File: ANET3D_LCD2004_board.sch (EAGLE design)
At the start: 15 parts

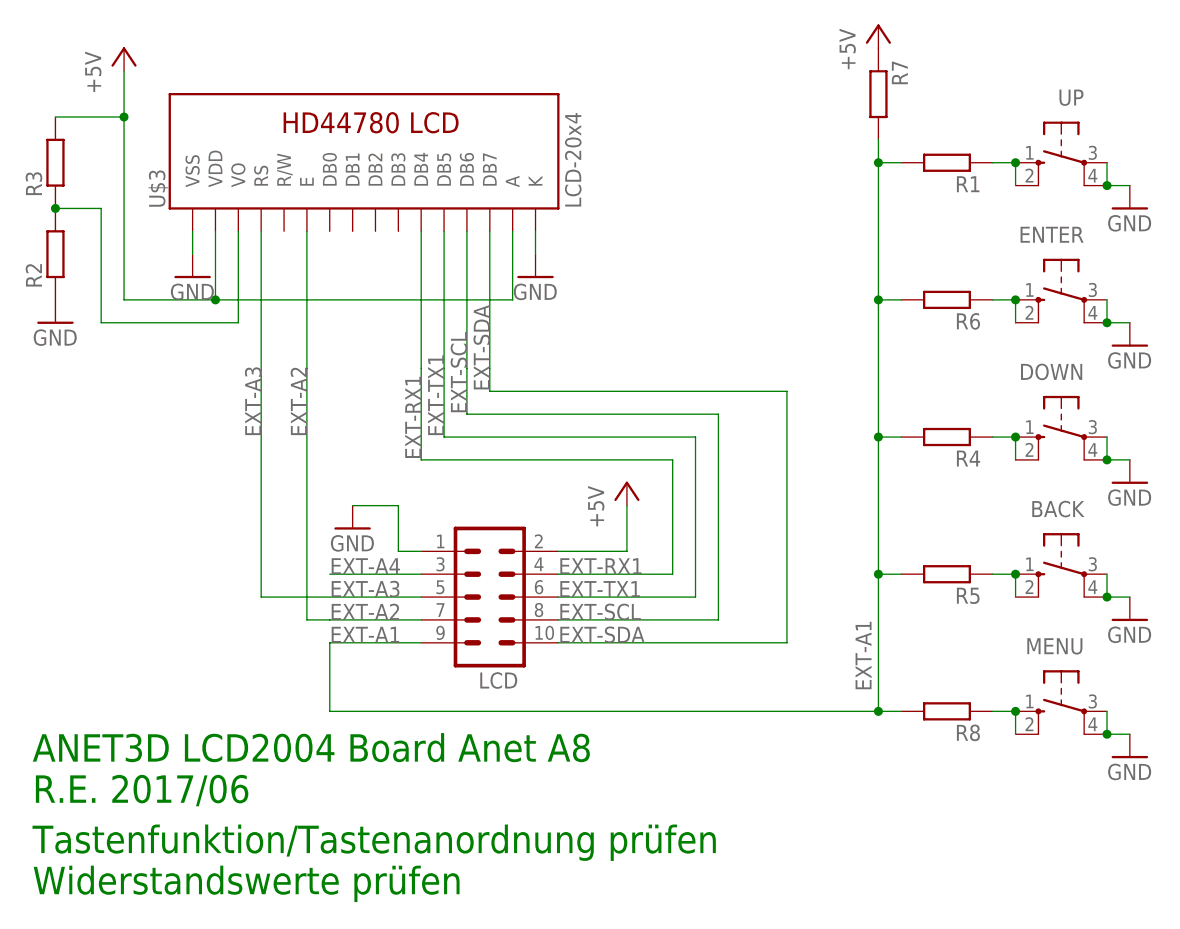
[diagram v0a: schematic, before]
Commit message: LCD2004 keypad resistor values
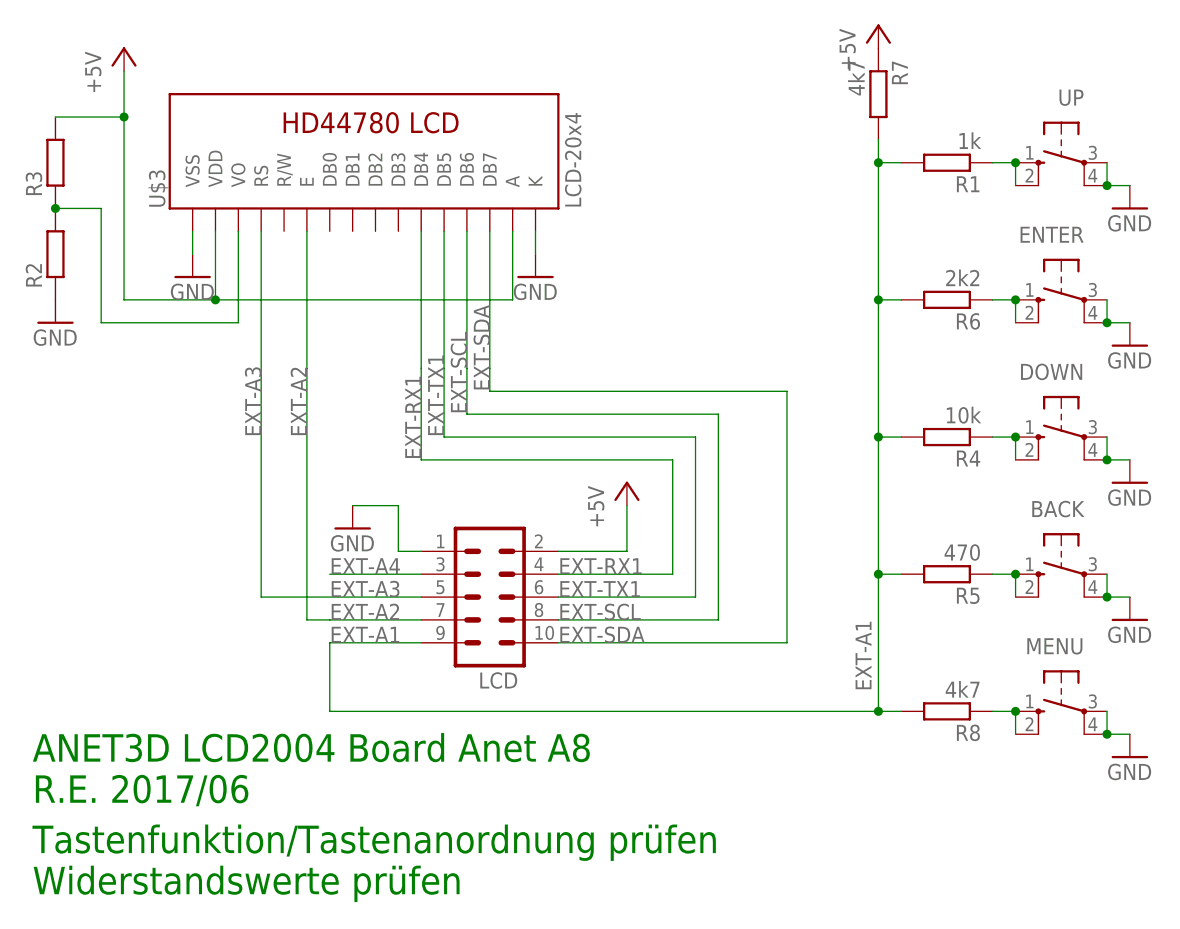
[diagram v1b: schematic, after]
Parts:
- R1: value (none) -> 1k
- R4: value (none) -> 10k
- R5: value (none) -> 470
- R6: value (none) -> 2k2
- R7, R8: value (none) -> 4k7
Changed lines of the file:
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@@
 <part name="R2" library="rcl" deviceset="R-EU_" device="R0805"/>
 <part name="R3" library="rcl" deviceset="R-EU_" device="R0805"/>
-<part name="R4" library="rcl" deviceset="R-EU_" device="R0805"/>
-<part name="R5" library="rcl" deviceset="R-EU_" device="R0805"/>
-<part name="R6" library="rcl" deviceset="R-EU_" device="R0805"/>
+<part name="R4" library="rcl" deviceset="R-EU_" device="R0805" value="10k"/>
+<part name="R5" library="rcl" deviceset="R-EU_" device="R0805" value="470"/>
+<part name="R6" library="rcl" deviceset="R-EU_" device="R0805" value="2k2"/>
 <part name="BACK" library="switch-omron" deviceset="40-XX" device=""/>
 <part name="MENU" library="switch-omron" deviceset="40-XX" device=""/>
@@
 <part name="UP" library="switch-omron" deviceset="40-XX" device=""/>
 <part name="DOWN" library="switch-omron" deviceset="40-XX" device=""/>
-<part name="R1" library="rcl" deviceset="R-EU_" device="R0805"/>
+<part name="R1" library="rcl" deviceset="R-EU_" device="R0805" value="1k"/>
 <part name="GND1" library="SparkFun" deviceset="GND" device=""/>
 <part name="GND2" library="SparkFun" deviceset="GND" device=""/>
@@
 <part name="GND8" library="SparkFun" deviceset="GND" device=""/>
 <part name="P+4" library="supply1" deviceset="+5V" device=""/>
-<part name="R8" library="rcl" deviceset="R-EU_" device="R0805"/>
-<part name="R7" library="rcl" deviceset="R-EU_" device="R0805"/>
+<part name="R8" library="rcl" deviceset="R-EU_" device="R0805" value="4k7"/>
+<part name="R7" library="rcl" deviceset="R-EU_" device="R0805" value="4k7"/>
 <part name="GND9" library="SparkFun" deviceset="GND" device=""/>
 <part name="GND10" library="SparkFun" deviceset="GND" device=""/>

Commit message: Anet3d LCD2004 Resistor values corrected
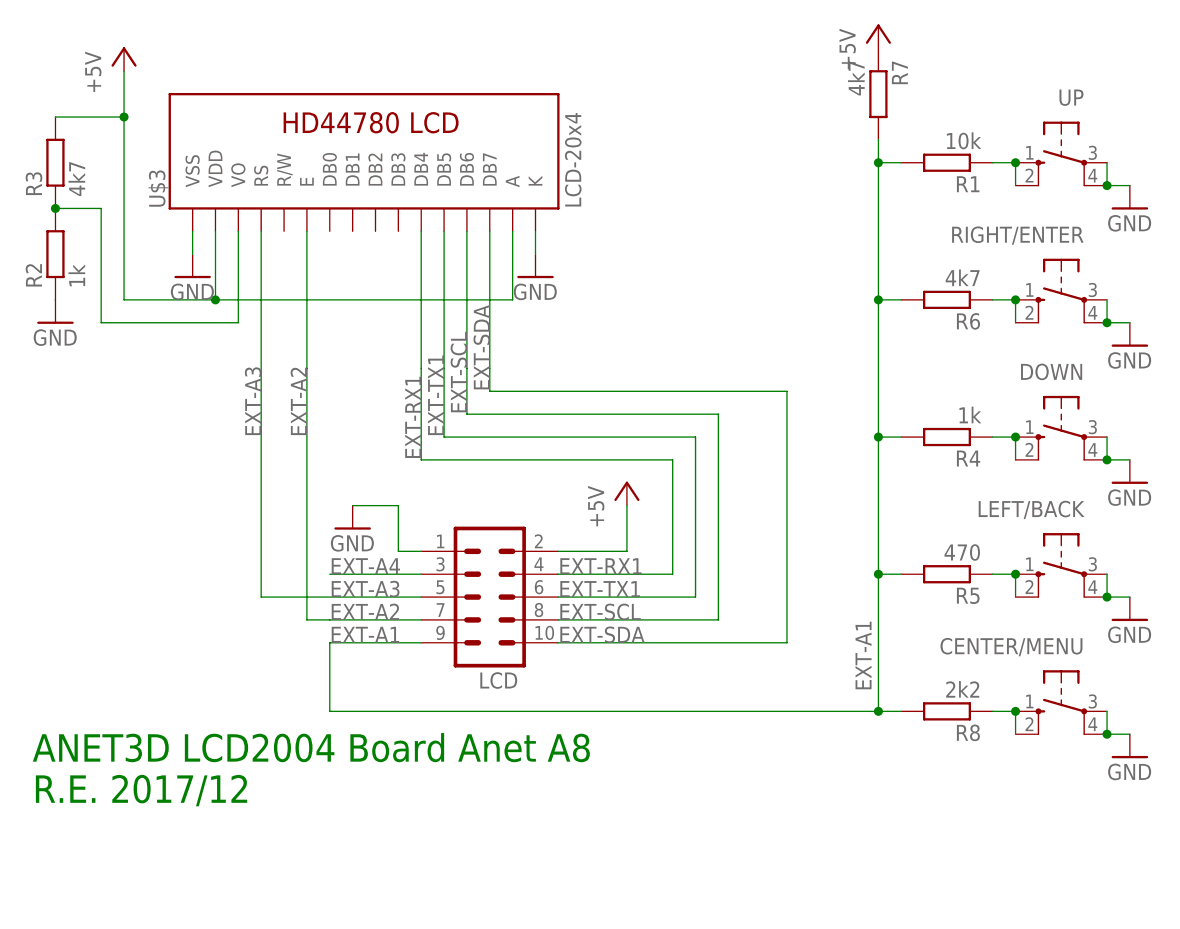
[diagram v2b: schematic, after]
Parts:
- R1: value 1k -> 10k
- R2: value (none) -> 1k
- R3: value (none) -> 4k7
- R4: value 10k -> 1k
- R6: value 2k2 -> 4k7
- R8: value 4k7 -> 2k2
- renumbered BACK to LEFT/BACK, ENTER to RIGHT/ENTER, MENU to CENTER/MENU
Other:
- note added: "ANET3D LCD2004 Board Anet A8 R.E. 2017/12"
- note removed: "ANET3D LCD2004 Board Anet A8 R.E. 2017/06"
- note removed: "Tastenfunktion/Tastenanordnung prüfen Widerstandswerte prüfen"
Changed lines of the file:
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@@
 <part name="P+2" library="supply1" deviceset="+5V" device=""/>
 <part name="U$3" library="HD44780LCD" deviceset="LCD-HD44780" device="20X4-4HOLES" technology="4-HOLES" value="LCD-20x4"/>
-<part name="R2" library="rcl" deviceset="R-EU_" device="R0805"/>
-<part name="R3" library="rcl" deviceset="R-EU_" device="R0805"/>
-<part name="R4" library="rcl" deviceset="R-EU_" device="R0805" value="10k"/>
+<part name="R2" library="rcl" deviceset="R-EU_" device="R0805" value="1k"/>
+<part name="R3" library="rcl" deviceset="R-EU_" device="R0805" value="4k7"/>
+<part name="R4" library="rcl" deviceset="R-EU_" device="R0805" value="1k"/>
 <part name="R5" library="rcl" deviceset="R-EU_" device="R0805" value="470"/>
-<part name="R6" library="rcl" deviceset="R-EU_" device="R0805" value="2k2"/>
-<part name="BACK" library="switch-omron" deviceset="40-XX" device=""/>
-<part name="MENU" library="switch-omron" deviceset="40-XX" device=""/>
-<part name="ENTER" library="switch-omron" deviceset="40-XX" device=""/>
+<part name="R6" library="rcl" deviceset="R-EU_" device="R0805" value="4k7"/>
+<part name="LEFT/BACK" library="switch-omron" deviceset="40-XX" device=""/>
+<part name="CENTER/MENU" library="switch-omron" deviceset="40-XX" device=""/>
+<part name="RIGHT/ENTER" library="switch-omron" deviceset="40-XX" device=""/>
 <part name="UP" library="switch-omron" deviceset="40-XX" device=""/>
 <part name="DOWN" library="switch-omron" deviceset="40-XX" device=""/>
-<part name="R1" library="rcl" deviceset="R-EU_" device="R0805" value="1k"/>
+<part name="R1" library="rcl" deviceset="R-EU_" device="R0805" value="10k"/>
 <part name="GND1" library="SparkFun" deviceset="GND" device=""/>
 <part name="GND2" library="SparkFun" deviceset="GND" device=""/>
@@
 <part name="GND8" library="SparkFun" deviceset="GND" device=""/>
 <part name="P+4" library="supply1" deviceset="+5V" device=""/>
-<part name="R8" library="rcl" deviceset="R-EU_" device="R0805" value="4k7"/>
+<part name="R8" library="rcl" deviceset="R-EU_" device="R0805" value="2k2"/>
 <part name="R7" library="rcl" deviceset="R-EU_" device="R0805" value="4k7"/>
 <part name="GND9" library="SparkFun" deviceset="GND" device=""/>
@@
 <plain>
 <text x="-10.16" y="27.94" size="3.048" layer="91" ratio="11">ANET3D LCD2004 Board Anet A8
-R.E. 2017/06</text>
-<text x="-10.16" y="17.78" size="3.048" layer="91" ratio="11">Tastenfunktion/Tastenanordnung prüfen
-Widerstandswerte prüfen</text>
+R.E. 2017/12</text>
 </plain>
 <instances>
@@
 <instance part="R5" gate="G$1" x="91.44" y="53.34" rot="R180"/>
 <instance part="R6" gate="G$1" x="91.44" y="83.82" rot="R180"/>
-<instance part="BACK" gate="1" x="104.14" y="53.34" rot="MR270"/>
-<instance part="MENU" gate="1" x="104.14" y="38.1" rot="MR270"/>
-<instance part="ENTER" gate="1" x="104.14" y="83.82" rot="MR270"/>
+<instance part="LEFT/BACK" gate="1" x="104.14" y="53.34" rot="MR270"/>
+<instance part="CENTER/MENU" gate="1" x="104.14" y="38.1" rot="MR270"/>
+<instance part="RIGHT/ENTER" gate="1" x="104.14" y="83.82" rot="MR270"/>
 <instance part="UP" gate="1" x="104.14" y="99.06" rot="MR270"/>
 <instance part="DOWN" gate="1" x="104.14" y="68.58" rot="MR270"/>
@@
 </segment>
 <segment>
-<pinref part="BACK" gate="1" pin="P"/>
-<pinref part="BACK" gate="1" pin="P1"/>
+<pinref part="LEFT/BACK" gate="1" pin="P"/>
+<pinref part="LEFT/BACK" gate="1" pin="P1"/>
 <wire x1="109.22" y1="53.34" x2="109.22" y2="50.8" width="0.1524" layer="91"/>
 <pinref part="GND2" gate="1" pin="GND"/>
@@
 <segment>
 <pinref part="GND5" gate="1" pin="GND"/>
-<pinref part="MENU" gate="1" pin="P1"/>
+<pinref part="CENTER/MENU" gate="1" pin="P1"/>
 <wire x1="111.76" y1="35.56" x2="109.22" y2="35.56" width="0.1524" layer="91"/>
-<pinref part="MENU" gate="1" pin="P"/>
+<pinref part="CENTER/MENU" gate="1" pin="P"/>
 <wire x1="109.22" y1="35.56" x2="109.22" y2="38.1" width="0.1524" layer="91"/>
 <junction x="109.22" y="35.56"/>
@@
 <segment>
 <pinref part="GND7" gate="1" pin="GND"/>
-<pinref part="ENTER" gate="1" pin="P1"/>
+<pinref part="RIGHT/ENTER" gate="1" pin="P1"/>
 <wire x1="111.76" y1="81.28" x2="109.22" y2="81.28" width="0.1524" layer="91"/>
-<pinref part="ENTER" gate="1" pin="P"/>
+<pinref part="RIGHT/ENTER" gate="1" pin="P"/>
 <wire x1="109.22" y1="81.28" x2="109.22" y2="83.82" width="0.1524" layer="91"/>
 <junction x="109.22" y="81.28"/>
@@
 <net name="N$4" class="0">
 <segment>
-<pinref part="BACK" gate="1" pin="S"/>
-<pinref part="BACK" gate="1" pin="S1"/>
+<pinref part="LEFT/BACK" gate="1" pin="S"/>
+<pinref part="LEFT/BACK" gate="1" pin="S1"/>
 <wire x1="99.06" y1="53.34" x2="99.06" y2="50.8" width="0.1524" layer="91"/>
 <pinref part="R5" gate="G$1" pin="1"/>
@@
 <net name="N$5" class="0">
 <segment>
-<pinref part="MENU" gate="1" pin="S"/>
-<pinref part="MENU" gate="1" pin="S1"/>
+<pinref part="CENTER/MENU" gate="1" pin="S"/>
+<pinref part="CENTER/MENU" gate="1" pin="S1"/>
 <wire x1="99.06" y1="38.1" x2="99.06" y2="35.56" width="0.1524" layer="91"/>
 <wire x1="96.52" y1="38.1" x2="99.06" y2="38.1" width="0.1524" layer="91"/>
@@
 <net name="N$6" class="0">
 <segment>
-<pinref part="ENTER" gate="1" pin="S"/>
-<pinref part="ENTER" gate="1" pin="S1"/>
+<pinref part="RIGHT/ENTER" gate="1" pin="S"/>
+<pinref part="RIGHT/ENTER" gate="1" pin="S1"/>
 <wire x1="99.06" y1="83.82" x2="99.06" y2="81.28" width="0.1524" layer="91"/>
 <pinref part="R6" gate="G$1" pin="1"/>
